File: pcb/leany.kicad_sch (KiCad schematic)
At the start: 39 parts, among them J1 ST7735S, J2 SWD, Q1 AO3401A, SW1 ZERO, SW2 HOLD, SW3 RESET, SW4 FLASH, U1 STM32F103C8Tx, U2 CH340C, U3 BMI270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

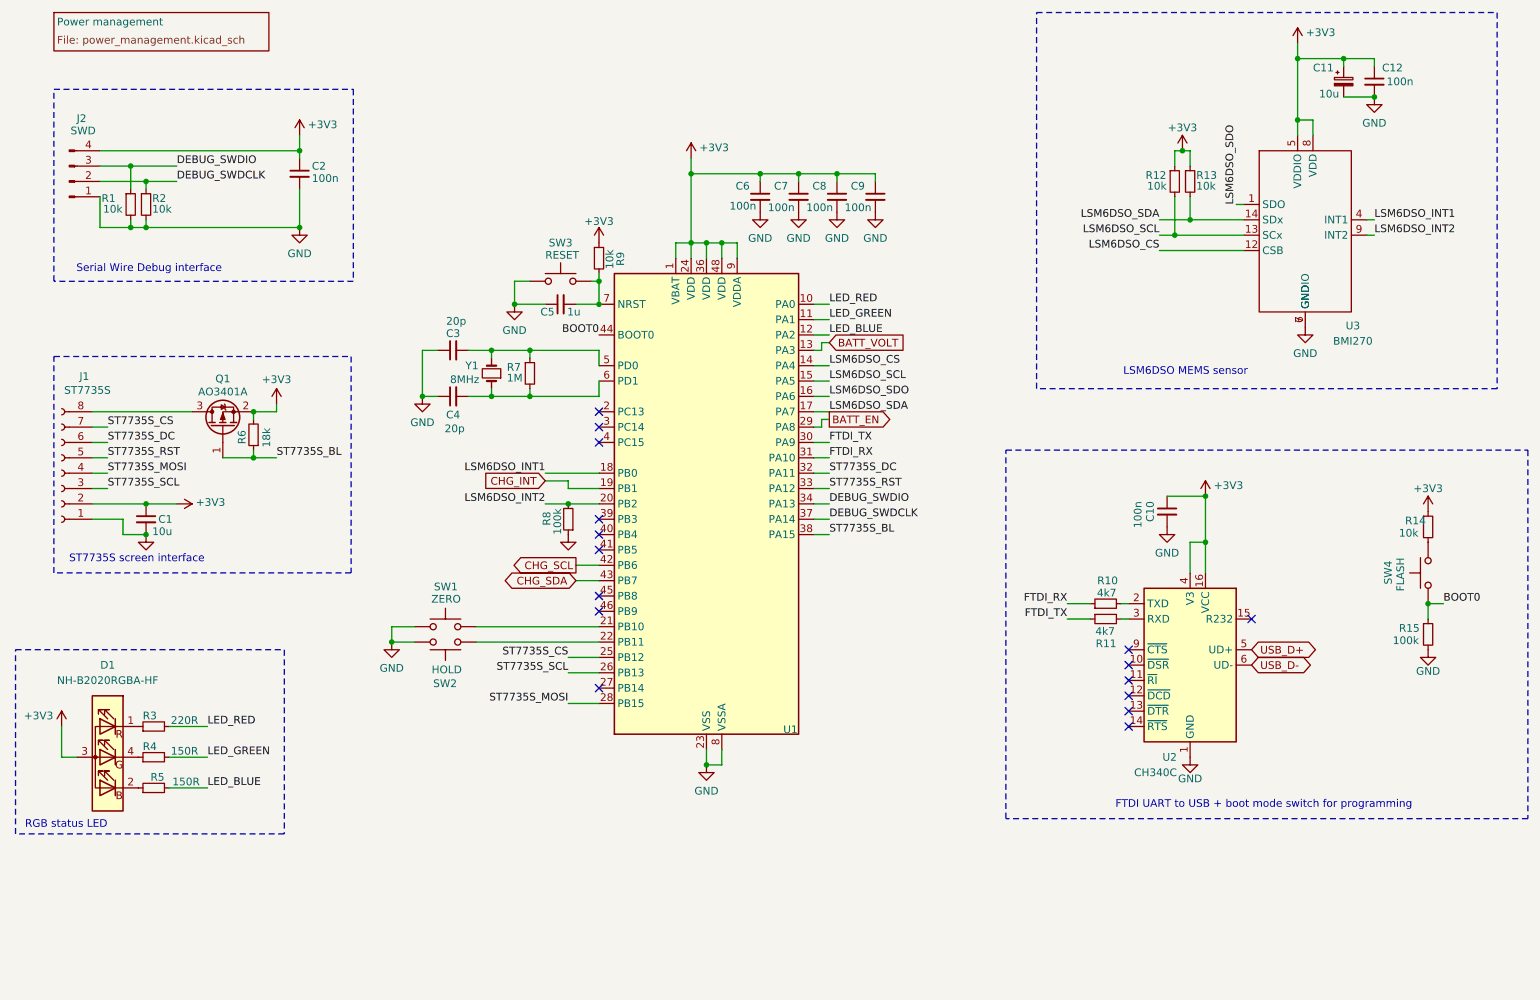
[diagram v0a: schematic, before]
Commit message: refactor: replace the LSM6DSO by a BMI270 (#5)
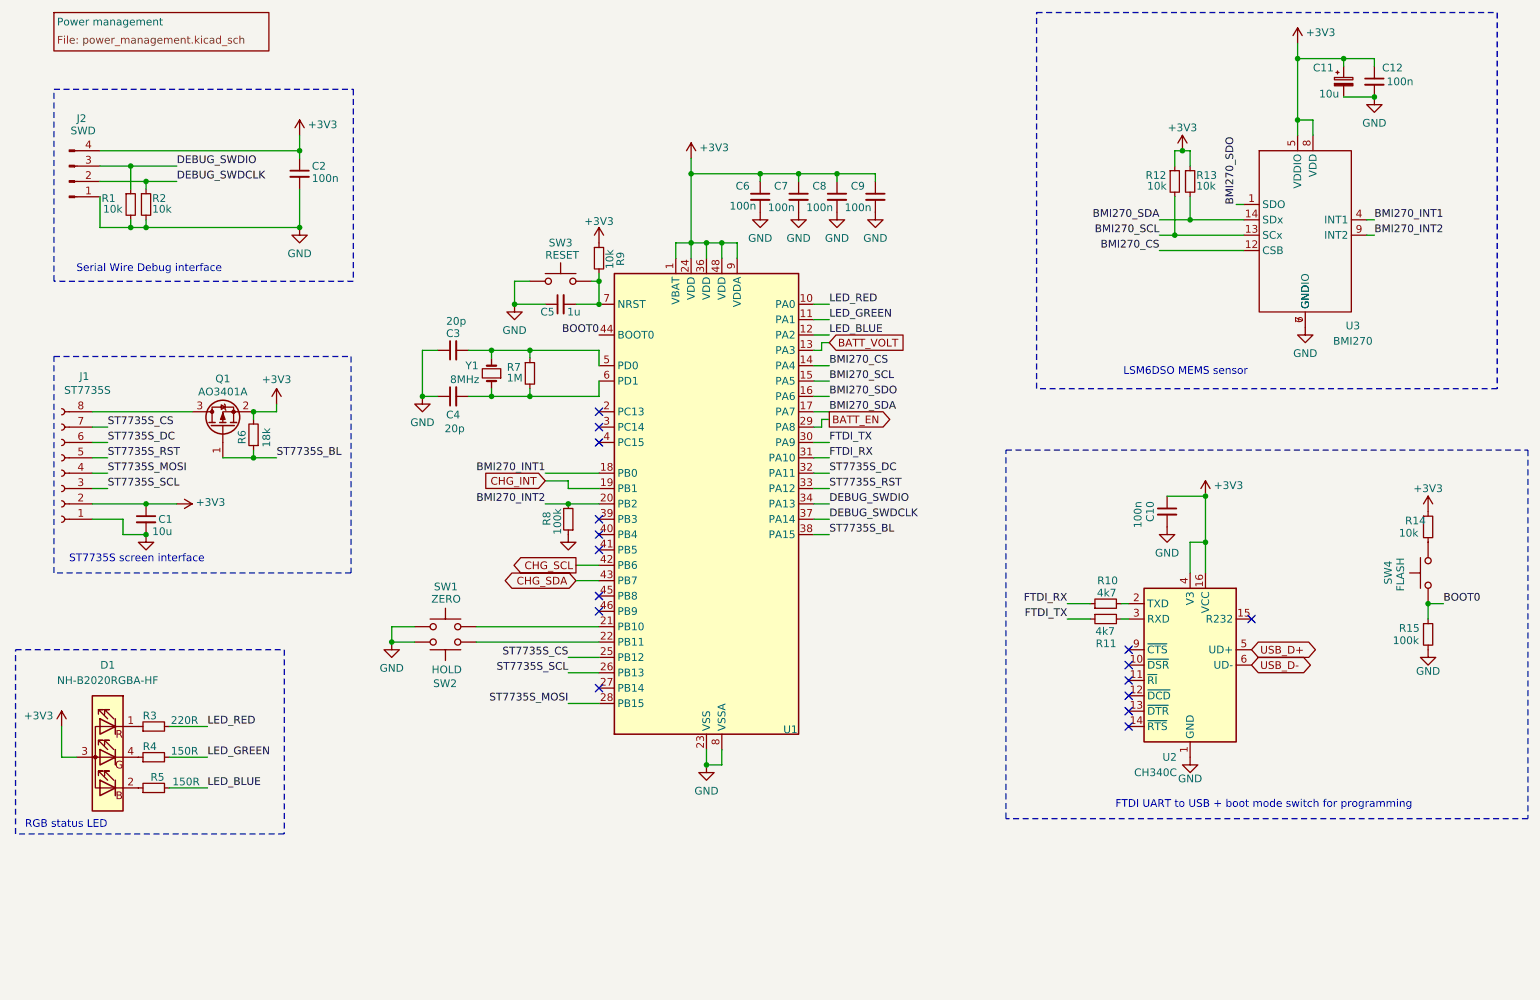
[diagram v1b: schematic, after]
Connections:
- net LSM6DSO_CS renamed BMI270_CS
- net LSM6DSO_INT1 renamed BMI270_INT1
- net LSM6DSO_INT2 renamed BMI270_INT2
- net LSM6DSO_SCL renamed BMI270_SCL
- net LSM6DSO_SDA renamed BMI270_SDA
- net LSM6DSO_SDO renamed BMI270_SDO
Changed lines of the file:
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@@
 	(title_block
 		(title "Leany")
-		(date "2025-02-12")
+		(date "2025-04-05")
 		(comment 1 "MIT License")
 		(comment 2 "Copyright (c) 2023 Gilles Henrard")
@@
 		)
 	)
-	(label "LSM6DSO_SDA"
+	(label "BMI270_SDA"
 		(at 153.67 86.36 0)
 		(effects
@@
 		)
 	)
-	(label "LSM6DSO_INT1"
+	(label "BMI270_INT1"
 		(at 106.68 96.52 180)
 		(effects
@@
 		)
 	)
-	(label "LSM6DSO_INT2"
+	(label "BMI270_INT2"
 		(at 106.68 101.6 180)
 		(effects
@@
 		)
 	)
-	(label "LSM6DSO_INT1"
+	(label "BMI270_INT1"
 		(at 243.84 54.61 0)
 		(effects
@@
 		)
 	)
-	(label "LSM6DSO_SCL"
+	(label "BMI270_SCL"
 		(at 208.28 57.15 180)
 		(effects
@@
 		)
 	)
-	(label "LSM6DSO_CS"
+	(label "BMI270_CS"
 		(at 153.67 78.74 0)
 		(effects
@@
 		)
 	)
-	(label "LSM6DSO_SCL"
+	(label "BMI270_SCL"
 		(at 153.67 81.28 0)
 		(effects
@@
 		)
 	)
-	(label "LSM6DSO_INT2"
+	(label "BMI270_INT2"
 		(at 243.84 57.15 0)
 		(effects
@@
 		)
 	)
-	(label "LSM6DSO_SDO"
+	(label "BMI270_SDO"
 		(at 220.98 52.07 90)
 		(effects
@@
 		)
 	)
-	(label "LSM6DSO_SDO"
+	(label "BMI270_SDO"
 		(at 153.67 83.82 0)
 		(effects
@@
 		)
 	)
-	(label "LSM6DSO_SDA"
+	(label "BMI270_SDA"
 		(at 208.28 54.61 180)
 		(effects
@@
 		)
 	)
-	(label "LSM6DSO_CS"
+	(label "BMI270_CS"
 		(at 208.28 59.69 180)
 		(effects

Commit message: perf: strenghen Mahony filter (#50)
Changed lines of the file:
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@@
 (kicad_sch
-	(version 20231120)
+	(version 20250114)
 	(generator "eeschema")
-	(generator_version "8.0")
+	(generator_version "9.0")
 	(paper "A4")
 	(title_block
@@
 		(comment 2 "Copyright (c) 2023 Gilles Henrard")
 	)
+	(rectangle
+		(start 19.05 125.73)
+		(end 63.5 156.21)
+		(stroke
+			(width 0)
+			(type dash)
+		)
+		(fill
+			(type none)
+		)
+	)
+	(rectangle
+		(start 187.96 20.32)
+		(end 264.16 82.55)
+		(stroke
+			(width 0)
+			(type dash)
+		)
+		(fill
+			(type none)
+		)
+	)
+	(rectangle
+		(start 25.4 33.02)
+		(end 74.93 64.77)
+		(stroke
+			(width 0)
+			(type dash)
+		)
+		(fill
+			(type none)
+		)
+	)
+	(rectangle
+		(start 182.88 92.71)
+		(end 269.24 153.67)
+		(stroke
+			(width 0)
+			(type dash)
+		)
+		(fill
+			(type none)
+		)
+	)
+	(rectangle
+		(start 25.4 77.216)
+		(end 74.549 113.03)
+		(stroke
+			(width 0)
+			(type dash)
+		)
+		(fill
+			(type none)
+		)
+	)
+	(text "FTDI UART to USB + boot mode switch for programming"
+		(exclude_from_sim no)
+		(at 225.552 151.384 0)
+		(effects
+			(font
+				(size 1.27 1.27)
+			)
+		)
+	)
+	(text "LSM6DSO MEMS sensor"
+		(exclude_from_sim no)
+		(at 212.598 79.756 0)
+		(effects
+			(font
+				(size 1.27 1.27)
+			)
+		)
+	)
+	(text "ST7735S screen interface"
+		(exclude_from_sim no)
+		(at 39.116 110.744 0)
+		(effects
+			(font
+				(size 1.27 1.27)
+			)
+		)
+	)
+	(text "RGB status LED"
+		(exclude_from_sim no)
+		(at 27.432 154.686 0)
+		(effects
+			(font
+				(size 1.27 1.27)
+			)
+		)
+	)
+	(text "Serial Wire Debug interface"
+		(exclude_from_sim no)
+		(at 41.148 62.738 0)
+		(effects
+			(font
+				(size 1.27 1.27)
+			)
+		)
+	)
 	(junction
 		(at 213.36 54.61)
@@
 		)
 	)
-	(rectangle
-		(start 19.05 125.73)
-		(end 63.5 156.21)
-		(stroke
-			(width 0)
-			(type dash)
-		)
-		(fill
-			(type none)
-		)
-	)
-	(rectangle
-		(start 187.96 20.32)
-		(end 264.16 82.55)
-		(stroke
-			(width 0)
-			(type dash)
-		)
-		(fill
-			(type none)
-		)
-	)
-	(rectangle
-		(start 25.4 33.02)
-		(end 74.93 64.77)
-		(stroke
-			(width 0)
-			(type dash)
-		)
-		(fill
-			(type none)
-		)
-	)
-	(rectangle
-		(start 182.88 92.71)
-		(end 269.24 153.67)
-		(stroke
-			(width 0)
-			(type dash)
-		)
-		(fill
-			(type none)
-		)
-	)
-	(rectangle
-		(start 25.4 77.216)
-		(end 74.549 113.03)
-		(stroke
-			(width 0)
-			(type dash)
-		)
-		(fill
-			(type none)
-		)
-	)
-	(text "FTDI UART to USB + boot mode switch for programming"
-		(exclude_from_sim no)
-		(at 225.552 151.384 0)
-		(effects
-			(font
-				(size 1.27 1.27)
-			)
-		)
-	)
-	(text "LSM6DSO MEMS sensor"
-		(exclude_from_sim no)
-		(at 212.598 79.756 0)
-		(effects
-			(font
-				(size 1.27 1.27)
-			)
-		)
-	)
-	(text "ST7735S screen interface"
-		(exclude_from_sim no)
-		(at 39.116 110.744 0)
-		(effects
-			(font
-				(size 1.27 1.27)
-			)
-		)
-	)
-	(text "RGB status LED"
-		(exclude_from_sim no)
-		(at 27.432 154.686 0)
-		(effects
-			(font
-				(size 1.27 1.27)
-			)
-		)
-	)
-	(text "Serial Wire Debug interface"
-		(exclude_from_sim no)
-		(at 41.148 62.738 0)
-		(effects
-			(font
-				(size 1.27 1.27)
-			)
-		)
-	)
 	(label "BMI270_SDA"
 		(at 153.67 86.36 0)
@@
 			)
 		)
-		(property "Datasheet" "https://jlcpcb.com/api/file/downloadByFileSystemAccessId/8550724022091735041"
+		(property "Datasheet" "~"
 			(at 247.65 113.03 0)
 			(effects
@@
 			)
 		)
-		(property "Description" "C318884"
+		(property "Description" "Push button switch, generic, two pins"
 			(at 252.73 113.03 0)
 			(effects
@@
 			)
 		)
-		(property "Datasheet" "https://jlcpcb.com/api/file/downloadByFileSystemAccessId/8550724022091735041"
+		(property "Datasheet" "~"
 			(at 109.22 59.69 0)
 			(effects
@@
 			)
 		)
-		(property "Description" "C318884"
+		(property "Description" "Push button switch, generic, two pins"
 			(at 109.22 64.77 0)
 			(effects
@@
 		(at 25.4 20.32)
 		(size 35.56 6.35)
+		(exclude_from_sim no)
+		(in_bom yes)
+		(on_board yes)
+		(dnp no)
 		(stroke
 			(width 0.1524)
@@
 		)
 	)
+	(embedded_fonts no)
 )

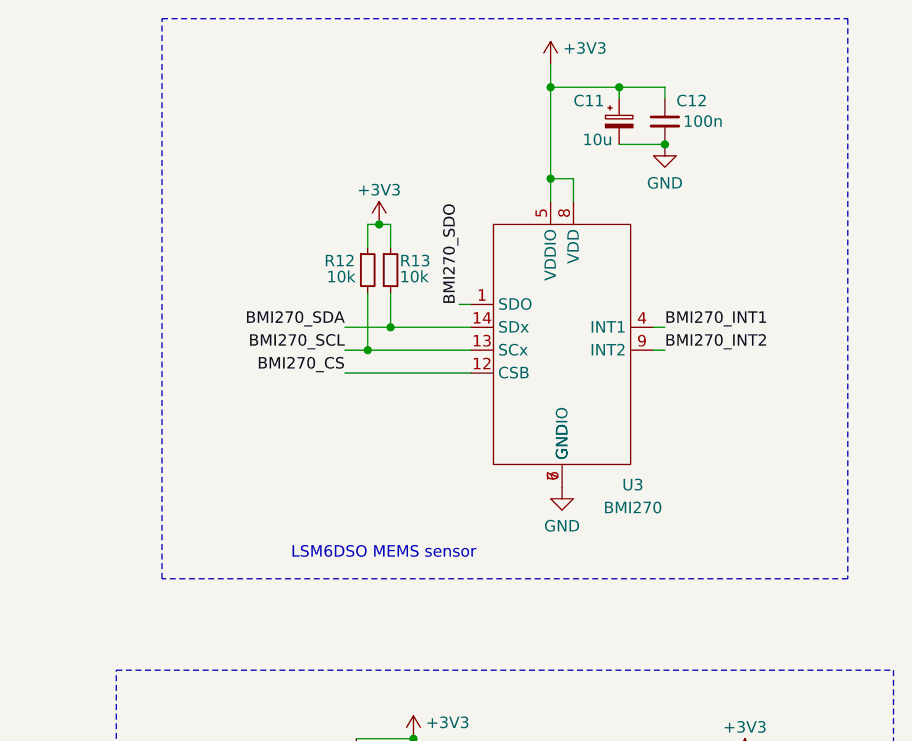
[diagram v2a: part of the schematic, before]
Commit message: remove SPI pull-ups
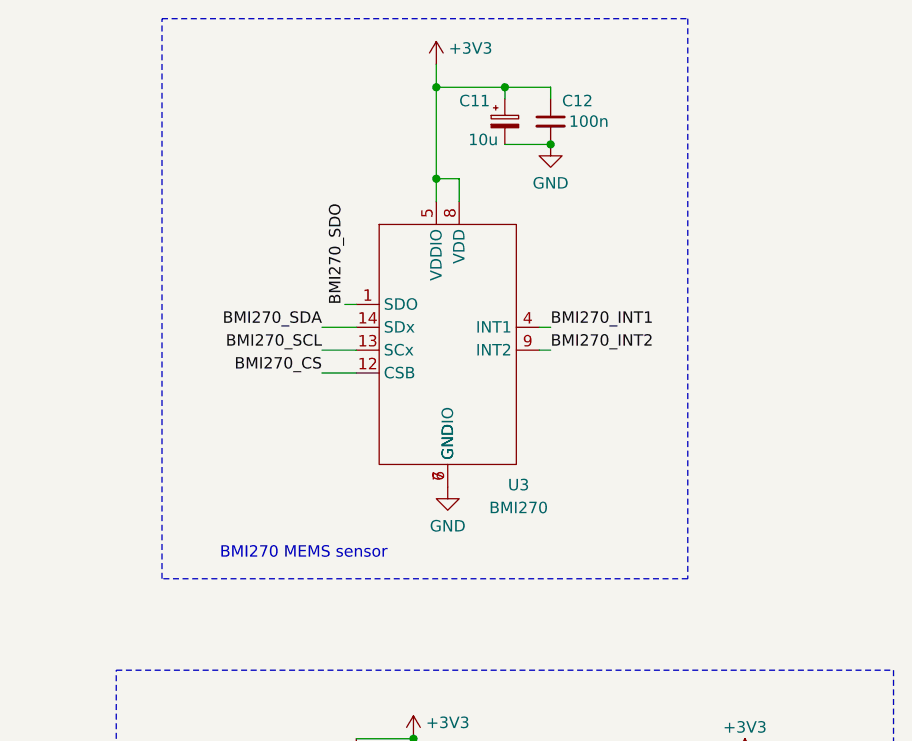
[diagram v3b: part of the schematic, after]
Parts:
- removed R12, R13: 10k, Resistor_SMD:R_0603_1608Metric, symbol Device:R_Small
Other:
- note added: "BMI270 MEMS sensor"
- note removed: "LSM6DSO MEMS sensor"
- moved on the sheet: C11, C12, U3

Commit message: update 3d models
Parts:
- SW3, SW4: footprint Button_Switch_SMD:SW_Push_1P1T_XKB_TS-1187A -> leany_footprints:SW_Push_1P1T_XKB_TS-1187A
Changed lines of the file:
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@@
 			)
 		)
-		(property "Footprint" "Button_Switch_SMD:SW_Push_1P1T_XKB_TS-1187A"
+		(property "Footprint" "leany_footprints:SW_Push_1P1T_XKB_TS-1187A"
 			(at 247.65 113.03 0)
 			(effects
@@
 			)
 		)
-		(property "Footprint" "Button_Switch_SMD:SW_Push_1P1T_XKB_TS-1187A"
+		(property "Footprint" "leany_footprints:SW_Push_1P1T_XKB_TS-1187A"
 			(at 109.22 59.69 0)
 			(effects

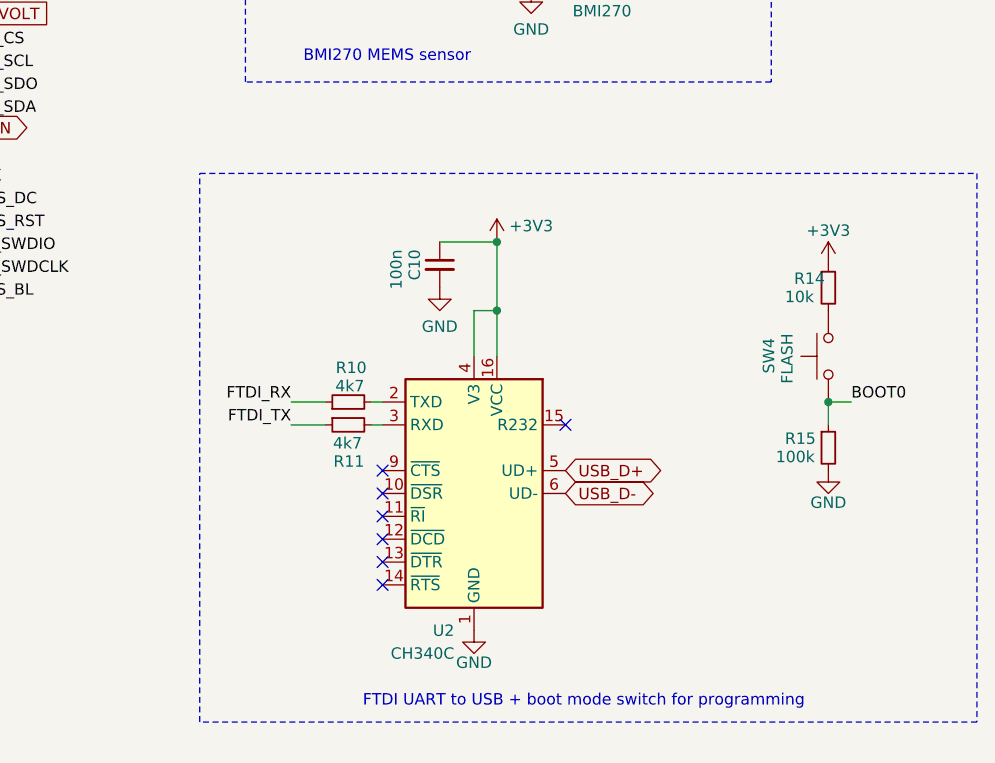
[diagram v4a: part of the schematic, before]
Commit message: change the CH340 to a CH340N
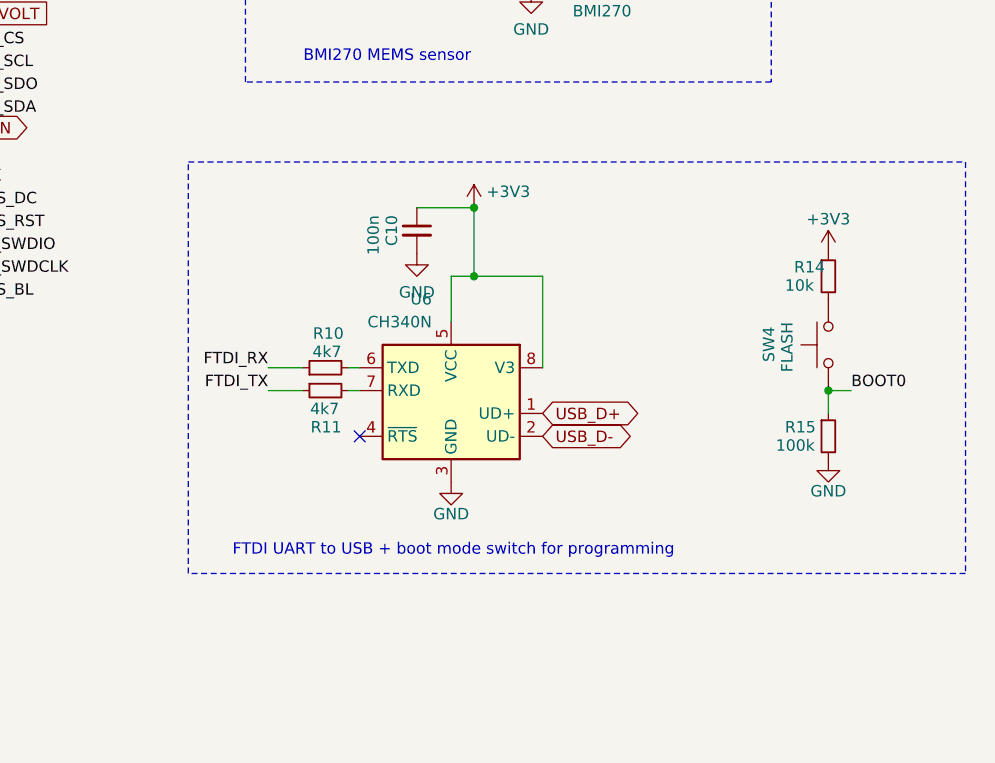
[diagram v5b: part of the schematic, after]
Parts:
- removed U2: CH340C, Package_SO:SOIC-16_3.9x9.9mm_P1.27mm, symbol leany-symbols:CH340C
- added U6: CH340N, leany_footprints:SOP-8_3.9x4.9mm_P1.27mm, symbol Interface_USB:CH340N
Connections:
- net +3V3: now also U6.5 (VCC), U6.8 (V3)
- net GND: now also U6.3 (GND)
- net USB_D+: now also U6.1 (UD+)
- net USB_D-: now also U6.2 (UD-)
- net at R10.2: now also U6.6 (TXD)
- net at R11.2: now also U6.7 (RXD)
- no-connect marks 16 -> 10
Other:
- moved on the sheet: C10, R10, R11, R14, R15, SW4
